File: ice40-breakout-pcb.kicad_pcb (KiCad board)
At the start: 2 copper layers, 55 parts, among them J1 USB_B_Micro, J2 USB_Break_Out, U1 SIT2001BI-S2-33E-12.000000G, U2 TLV73333PDBV, U3 TLV73312PDBV, U4 AT25SF081-SHD-X, U5 ICE40HX4K-TQ144

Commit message: Allocate FPGA pins for LED & USB.
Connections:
- U5 pad 129: Net-(U5-Pad129) -> CLK
- U5 pad 47: Net-(U5-Pad47) -> USB_N
- U5 pad 48: Net-(U5-Pad48) -> USB_P
- U5 pad 49: Net-(U5-Pad49) -> USB_PU

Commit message: Make it easier to route PLL grounds.
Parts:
- moved C7 1.91 mm to (120.0, 76.7), turned to 180 degrees
- moved C1 1.77 mm to (119.5, 104.0), turned to 180 degrees
- moved C2 1.77 mm to (119.5, 106.5), turned to 180 degrees
- moved C8 1.70 mm to (120.0, 74.2), turned to 180 degrees

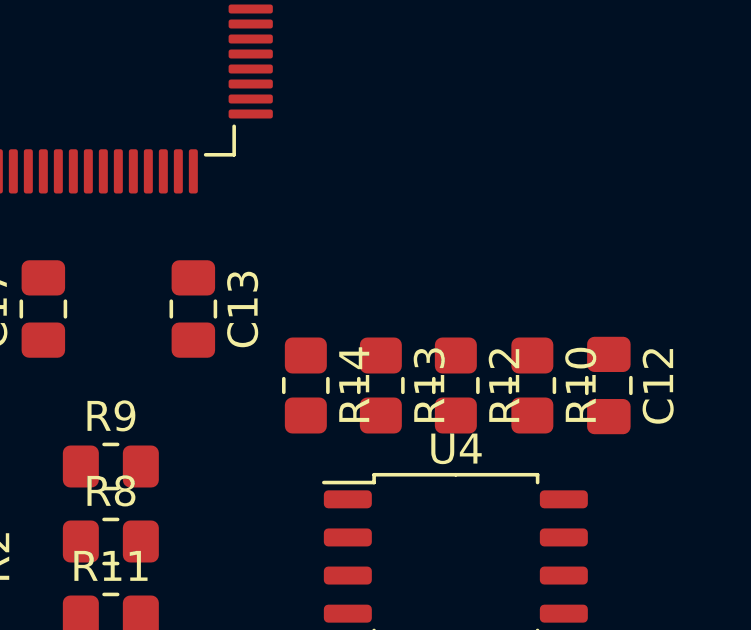
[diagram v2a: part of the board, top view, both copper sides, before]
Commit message: Re-position SCK pull-up to give SS a path to connector.
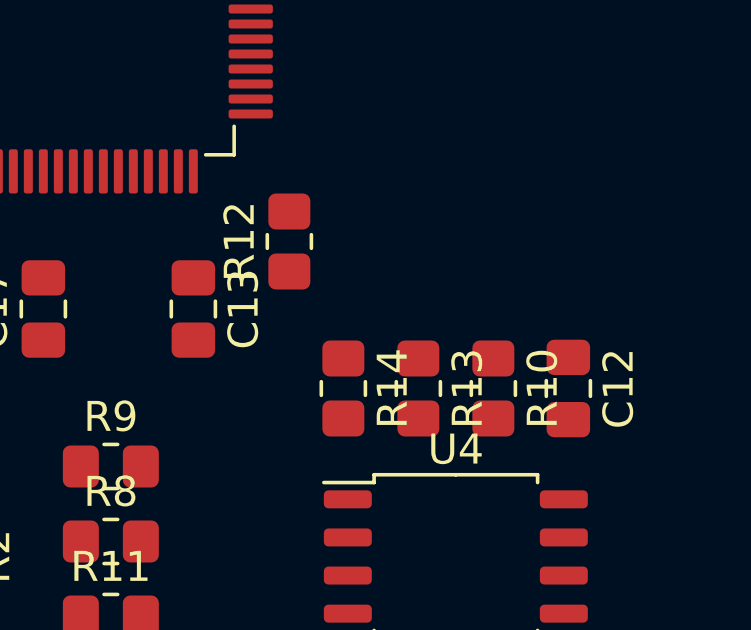
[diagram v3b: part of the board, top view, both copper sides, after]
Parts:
- moved R12 7.34 mm to (131.9, 103.0), turned to 90 degrees
- moved C12 1.35 mm to (141.2, 107.9)
- moved R10 1.30 mm to (138.8, 107.9)
- moved R13 1.25 mm to (136.2, 107.9)
- moved R14 1.25 mm to (133.8, 107.9)
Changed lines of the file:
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@@
   )
   (module Capacitor_SMD:C_0805_2012Metric_Pad1.18x1.45mm_HandSolder (layer F.Cu)
-    (at 142.6 107.8 270)
+    (at 141.25 107.9 270)
     (descr "Capacitor SMD 0805 (2012 Metric), square (rectangular) end terminal, IPC_7351 nominal with elongated pad for handsoldering. (Body size source: IPC-SM-782 page 76, https://www.pcb-3d.com/wordpress/wp-content/uploads/ipc-sm-782a_amendment_1_and_2.pdf, https://docs.google.com/spreadsheets/d/1BsfQQcO9C6DZCsRaXUlFlo91Tg2WpOkGARC1WS5S8t0/edit?usp=sharing), generated with kicad-footprint-generator")
     (tags "capacitor handsolder")
@@
   )
   (module Resistor_SMD:R_0805_2012Metric_Pad1.20x1.40mm_HandSolder (layer F.Cu)
-    (at 137.5 107.8 270)
+    (at 131.95 103 90)
     (descr "Resistor SMD 0805 (2012 Metric), square (rectangular) end terminal, IPC_7351 nominal with elongated pad for handsoldering. (Body size source: IPC-SM-782 page 72, https://www.pcb-3d.com/wordpress/wp-content/uploads/ipc-sm-782a_amendment_1_and_2.pdf), generated with kicad-footprint-generator")
     (tags "resistor handsolder")
@@
       (effects (font (size 0.5 0.5) (thickness 0.08)))
     )
-    (pad 2 smd roundrect (at 1 0 270) (size 1.2 1.4) (layers F.Cu F.Paste F.Mask) (roundrect_rratio 0.208333)
+    (pad 2 smd roundrect (at 1 0 90) (size 1.2 1.4) (layers F.Cu F.Paste F.Mask) (roundrect_rratio 0.208333)
       (net 20 SPI_SCK))
-    (pad 1 smd roundrect (at -1 0 270) (size 1.2 1.4) (layers F.Cu F.Paste F.Mask) (roundrect_rratio 0.208333)
+    (pad 1 smd roundrect (at -1 0 90) (size 1.2 1.4) (layers F.Cu F.Paste F.Mask) (roundrect_rratio 0.208333)
       (net 3 +3V3))
     (model ${KISYS3DMOD}/Resistor_SMD.3dshapes/R_0805_2012Metric.wrl
@@
   )
   (module Resistor_SMD:R_0805_2012Metric_Pad1.20x1.40mm_HandSolder (layer F.Cu)
-    (at 135 107.8 270)
+    (at 136.25 107.9 270)
     (descr "Resistor SMD 0805 (2012 Metric), square (rectangular) end terminal, IPC_7351 nominal with elongated pad for handsoldering. (Body size source: IPC-SM-782 page 72, https://www.pcb-3d.com/wordpress/wp-content/uploads/ipc-sm-782a_amendment_1_and_2.pdf), generated with kicad-footprint-generator")
     (tags "resistor handsolder")
@@
   )
   (module Resistor_SMD:R_0805_2012Metric_Pad1.20x1.40mm_HandSolder (layer F.Cu)
-    (at 132.5 107.8 270)
+    (at 133.75 107.9 270)
     (descr "Resistor SMD 0805 (2012 Metric), square (rectangular) end terminal, IPC_7351 nominal with elongated pad for handsoldering. (Body size source: IPC-SM-782 page 72, https://www.pcb-3d.com/wordpress/wp-content/uploads/ipc-sm-782a_amendment_1_and_2.pdf), generated with kicad-footprint-generator")
     (tags "resistor handsolder")
@@
   )
   (module Resistor_SMD:R_0805_2012Metric_Pad1.20x1.40mm_HandSolder (layer F.Cu)
-    (at 140.05 107.8 270)
-    (descr "Resistor SMD 0805 (2012 Metric), square (rectangular) end terminal, IPC_7351 nominal with elongated pad for handsoldering. (Body size source: IPC-SM-782 page 72, https://www.pcb-3d.com/wordpress/wp-content/uploads/ipc-sm-782a_amendment_1_and_2.pdf), generated with kicad-footprint-generator")
-    (tags "resistor handsolder")
+    (at 138.75 107.9 270)
+    (descr "Resistor SMD 0805 (2012 Metric), square (rectangular) end terminal, IPC_7351 nominal with elongated pad for handsoldering. (Body size source: IPC-SM-782 page 72, https://www.pcb-3d.com/wordpress/wp-content/uploads/ipc-sm-782a_amendment_1_and_2.pdf), generated with kicad-footprint-generator")
+    (tags "resistor handsolder")

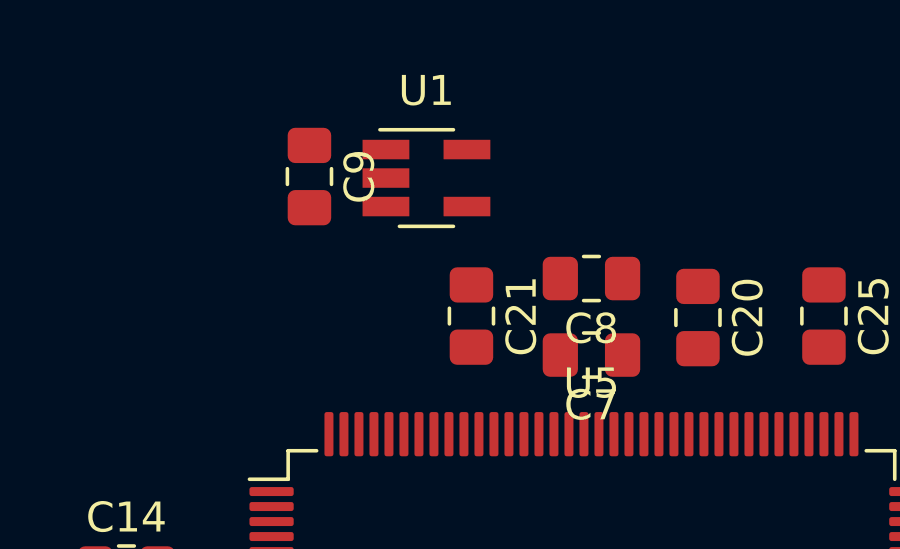
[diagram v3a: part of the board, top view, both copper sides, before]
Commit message: Place cap next to power pin.
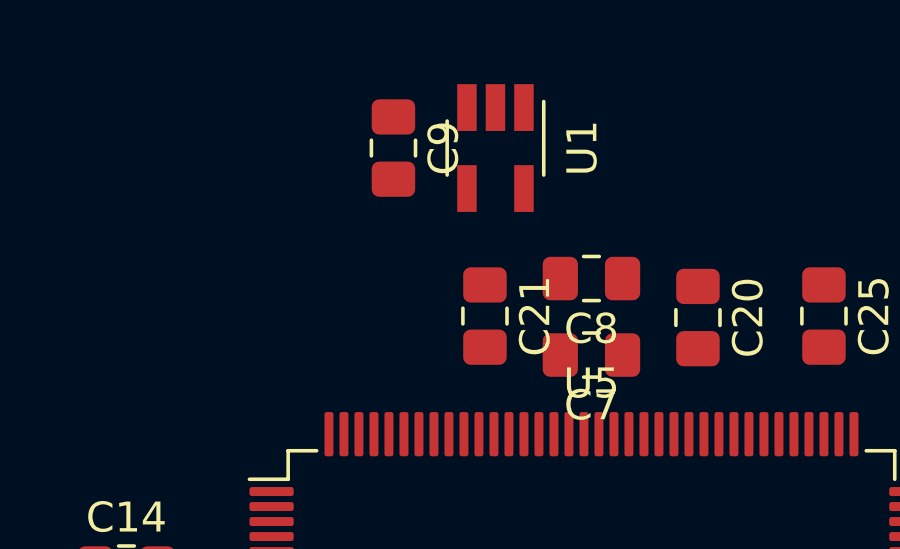
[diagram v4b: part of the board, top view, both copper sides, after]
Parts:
- moved C9 2.96 mm to (113.4, 69.8)
- moved U1 2.51 mm to (116.8, 69.8), turned to 270 degrees
- moved C21 0.45 mm to (116.5, 75.4)

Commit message: Allocate FPGA pin for LED.
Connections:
- U5 pad 41: Net-(U5-Pad41) -> LED

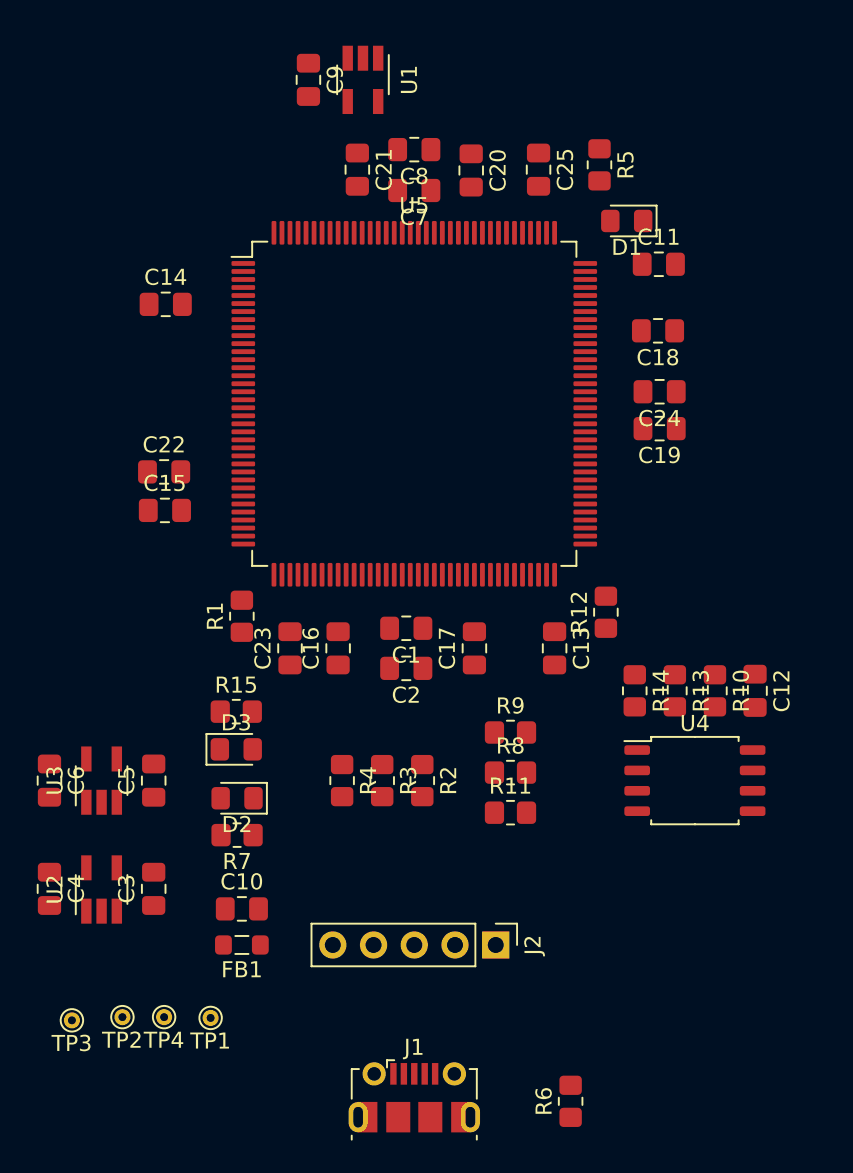
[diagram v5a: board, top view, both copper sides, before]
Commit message: Adjust component placement for easy soldering.
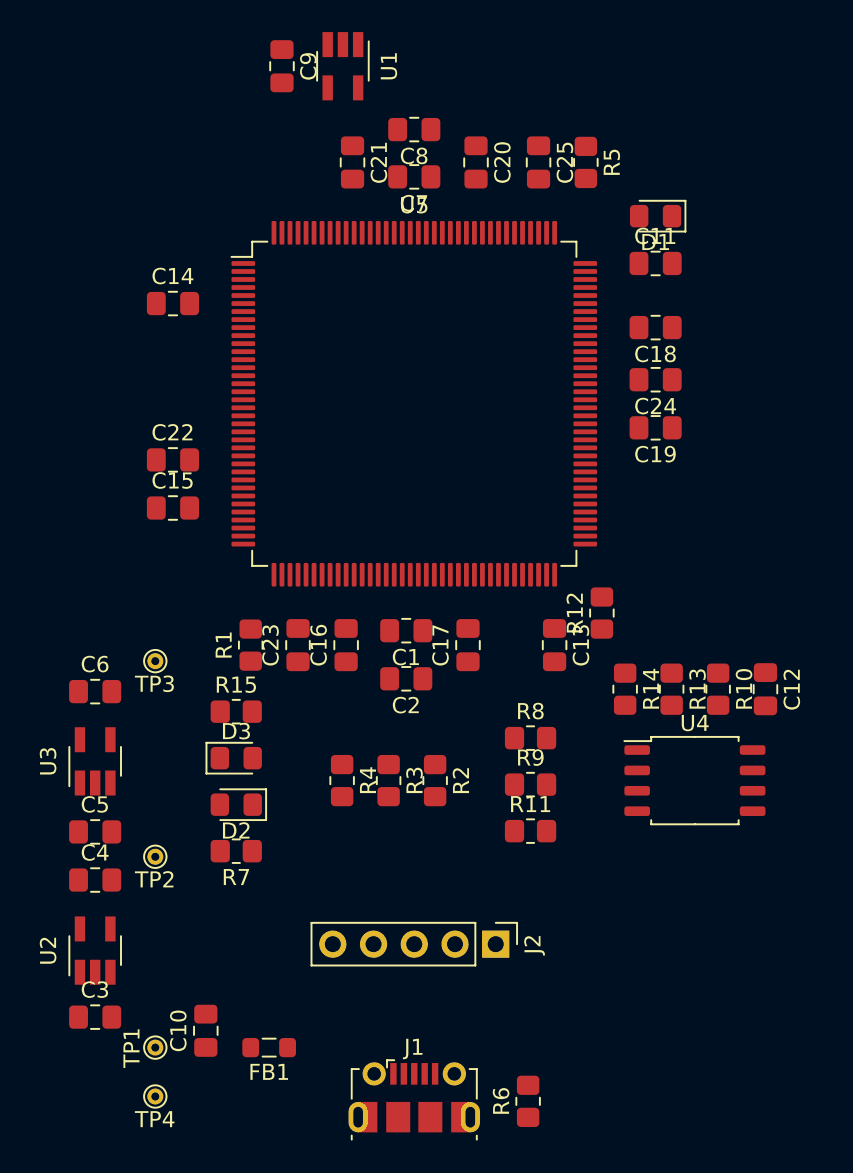
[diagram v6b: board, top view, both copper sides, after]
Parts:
- moved TP3 23.0 mm to (103.8, 106.0)
- moved TP2 10.2 mm to (103.8, 118.2)
- moved C3 8.79 mm to (100.1, 128.2), turned to 0 degrees
- moved C10 7.93 mm to (107.0, 129.1), turned to 90 degrees
- moved FB1 6.62 mm to (111.0, 130.2)
- moved C6 6.24 mm to (100.1, 108.0), turned to 0 degrees
- moved TP4 4.98 mm to (103.8, 133.2)
- moved C5 4.85 mm to (100.1, 116.7), turned to 0 degrees
- moved TP1 3.91 mm to (103.8, 130.2), turned to 90 degrees
- moved U2 3.83 mm to (100.1, 124.1)
- moved R9 3.48 mm to (127.2, 113.8)
- moved C4 2.90 mm to (100.1, 119.7), turned to 0 degrees
- moved R6 2.65 mm to (127.1, 133.5)
- moved R8 2.49 mm to (127.2, 110.8)
- moved R1 1.88 mm to (109.8, 105.0)
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
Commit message: Tweak board set-up. (Trace widths, etc.)
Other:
- net class Default: clearance 0.2 -> 0.18; trace_width 0.25 -> 0.18
- net class Power added: clearance 0.18, trace_width 0.3, via_dia 0.8, via_drill 0.4
- rule trace_clearance: 0.2 -> 0.18
- rule trace_min: 0.2 -> 0.127
- rule via_min_drill: 0.3 -> 0.2
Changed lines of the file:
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@@
   )
   (setup
-    (last_trace_width 0.25)
-    (trace_clearance 0.2)
+    (last_trace_width 0.18)
+    (trace_clearance 0.18)
     (zone_clearance 0.508)
     (zone_45_only no)
-    (trace_min 0.2)
+    (trace_min 0.127)
     (via_size 0.8)
     (via_drill 0.4)
     (via_min_size 0.4)
-    (via_min_drill 0.3)
+    (via_min_drill 0.2)
     (uvia_size 0.3)
     (uvia_drill 0.1)
@@
   (net 138 "Net-(D3-Pad1)")
   (net_class Default "This is the default net class."
-    (clearance 0.2)
-    (trace_width 0.25)
+    (clearance 0.18)
+    (trace_width 0.18)
     (via_dia 0.8)
     (via_drill 0.4)
     (uvia_dia 0.3)
     (uvia_drill 0.1)
-    (add_net +1V2)
-    (add_net +3V3)
-    (add_net +5V)
     (add_net CDONE)
     (add_net CLK)
     (add_net CRESET)
-    (add_net GND)
-    (add_net GNDPLL0)
-    (add_net GNDPLL1)
     (add_net LED)
     (add_net "Net-(D2-Pad1)")
     (add_net "Net-(D3-Pad1)")
-    (add_net "Net-(FB1-Pad1)")
     (add_net "Net-(J1-Pad2)")
     (add_net "Net-(J1-Pad3)")
@@
     (add_net USB_P)
     (add_net USB_PU)
+  )
+  (net_class Power ""
+    (clearance 0.18)
+    (trace_width 0.3)
+    (via_dia 0.8)
+    (via_drill 0.4)
+    (uvia_dia 0.3)
+    (uvia_drill 0.1)
+    (add_net +1V2)
+    (add_net +3V3)
+    (add_net +5V)
+    (add_net GND)
+    (add_net GNDPLL0)
+    (add_net GNDPLL1)
+    (add_net "Net-(FB1-Pad1)")
     (add_net VCCPLL0)
     (add_net VCCPLL1)

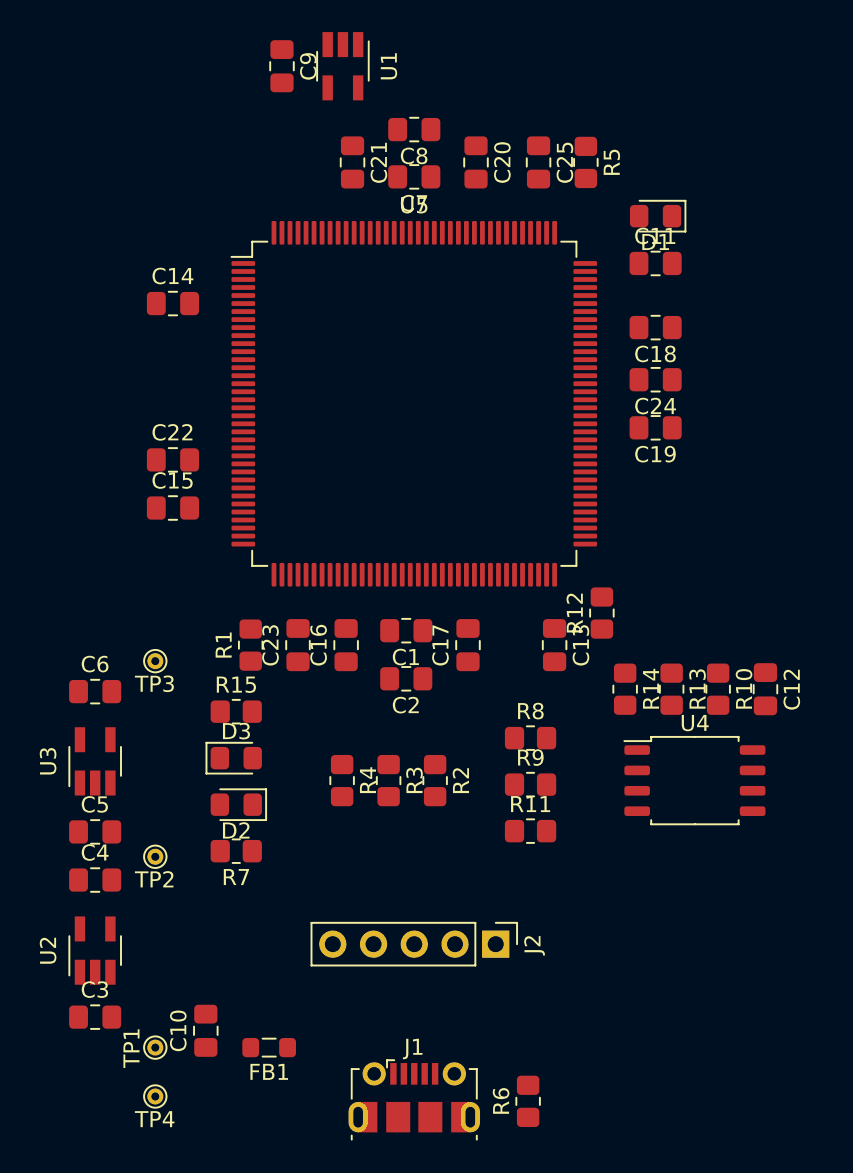
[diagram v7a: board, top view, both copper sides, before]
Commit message: First pass at routing for core.
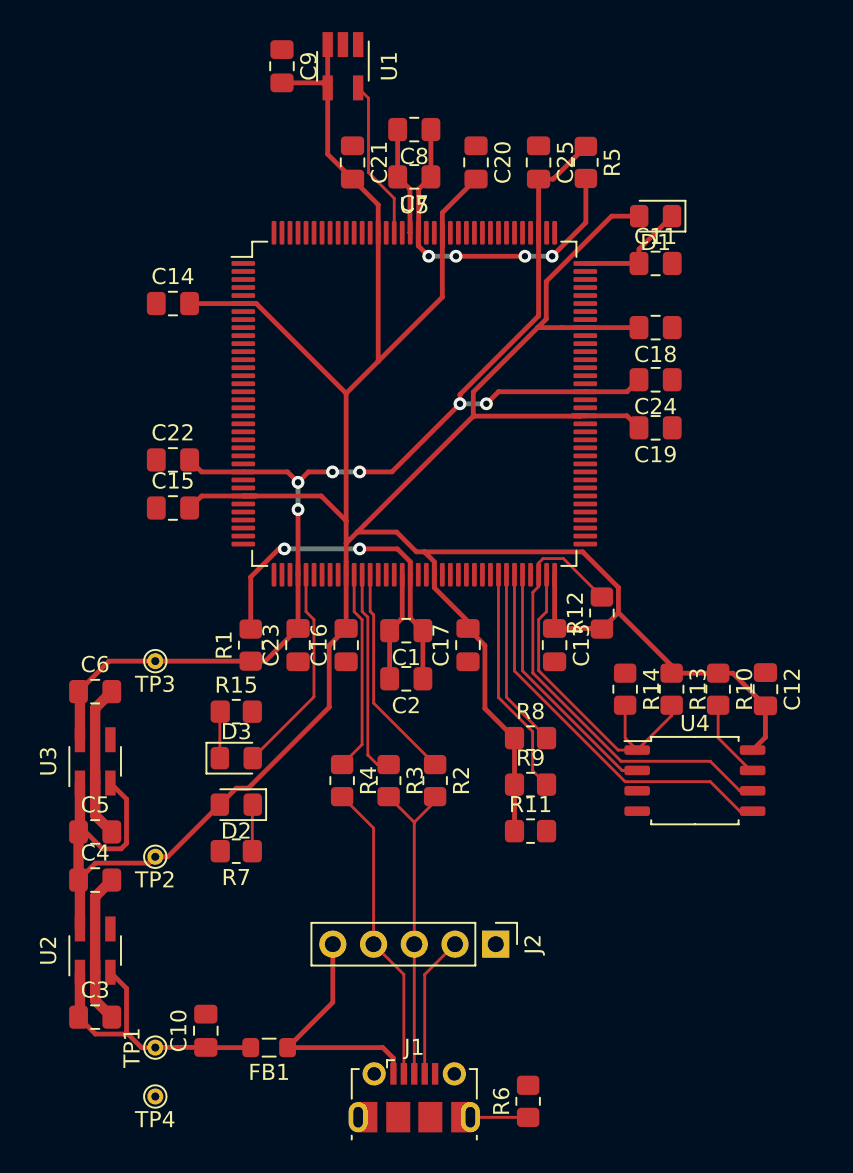
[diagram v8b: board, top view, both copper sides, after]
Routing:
- net +3V3: track 0.00 -> 230.7 mm
- net +1V2: track 0.00 -> 78.6 mm, vias 0 -> 6
- net SPI_SCK: track 0.00 -> 28.8 mm
- net SPI_MOSI: track 0.00 -> 24.5 mm
- net VCCPLL1: track 0.00 -> 21.9 mm, vias 0 -> 4
- net VCCPLL0: track 0.00 -> 21.9 mm, vias 0 -> 2
- net SPI_SS: track 0.00 -> 21.2 mm
- net Net-(J1-Pad3): track 0.00 -> 20.1 mm
- net GND: track 0.00 -> 19.0 mm
- net Net-(J1-Pad2): track 0.00 -> 18.9 mm
- net +5V: track 0.00 -> 18.7 mm
- net SPI_MISO: track 0.00 -> 15.7 mm
- net Net-(FB1-Pad1): track 0.00 -> 15.5 mm
- net CDONE: track 0.00 -> 14.3 mm
- net USB_PU: track 0.00 -> 13.5 mm
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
